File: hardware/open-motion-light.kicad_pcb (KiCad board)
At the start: 2 copper layers, 77 x 73 mm, 89 parts, among them J1 TYPE-C-31-M-12, J2 Conn_01x04, Q1 2N7002, SW1 SW_Push, SW2 SW_Push, SW3 SSSS213800, U1 CN3058E, U2 STM32L031G6U6, U3 MT9284BS6, U4 PIR223D-S0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

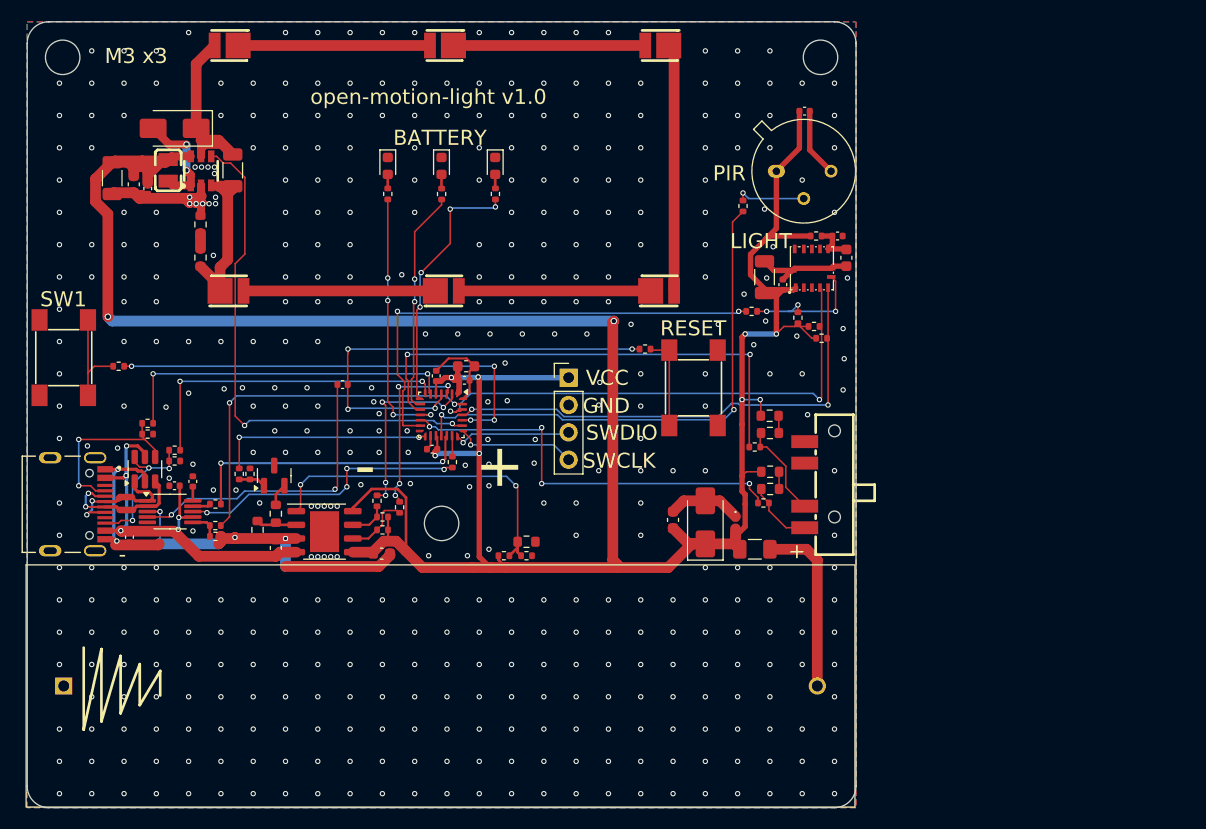
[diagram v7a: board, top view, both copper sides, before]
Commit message: Start updating placement and routing for v1.1
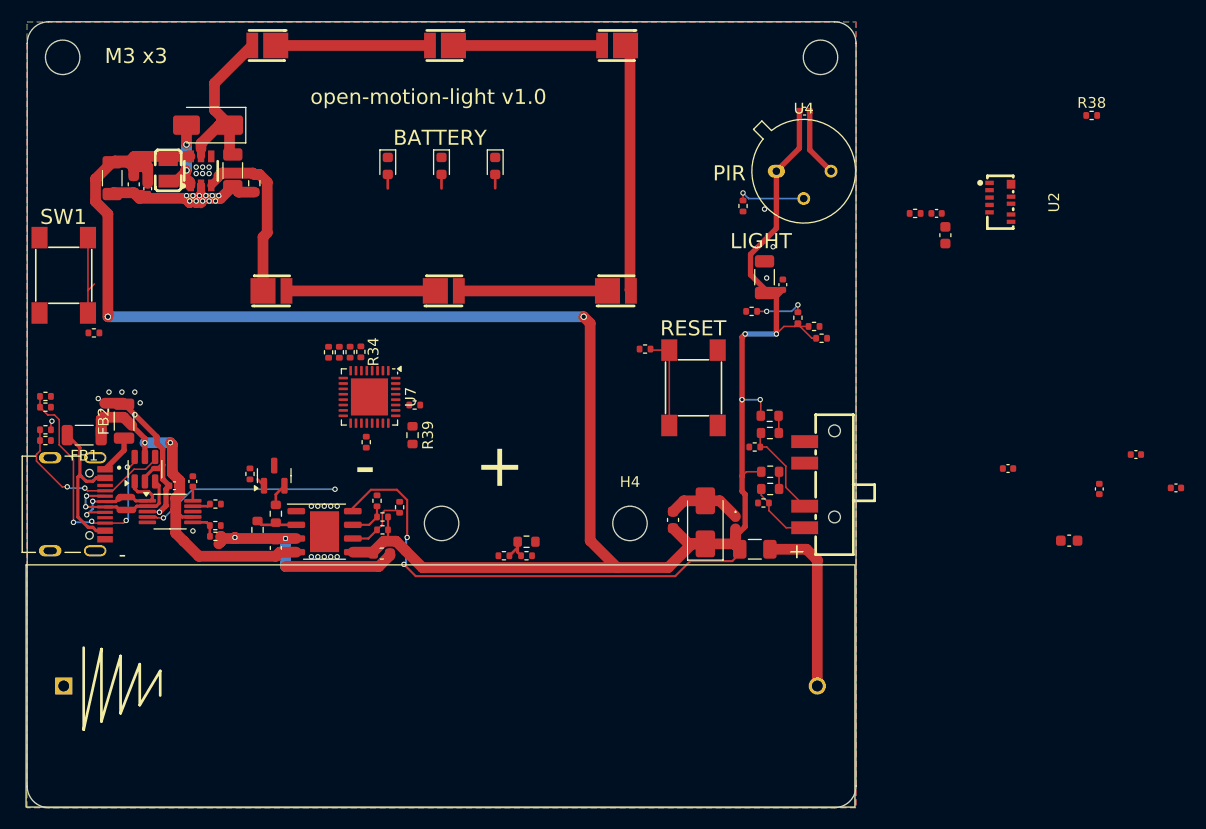
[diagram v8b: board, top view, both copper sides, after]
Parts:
- removed J2: Conn_01x04, Connector_PinHeader_2.54mm:PinHeader_1x04_P2.54mm_Vertical
- removed U5: VCNL4010-GS08, Homebrew:SENSORS-SMD_VCNL4010-GS08
- added FB1: 0R, Inductor_SMD:L_1206_3216Metric, F.Cu at (56.3, 101.4)
- added FB2: 0R, Inductor_SMD:L_1206_3216Metric, F.Cu at (60.0, 100.1)
- added H4: MountingHole, MountingHole:MountingHole_3.2mm_M3_ISO7380, F.Cu at (107.0, 109.6)
- added R38: 100k, Resistor_SMD:R_0402_1005Metric, F.Cu at (149.9, 71.7)
- added R39: 2M, Resistor_SMD:R_0603_1608Metric, F.Cu at (86.8, 101.4)
- added U7: STM32L051K8Ux, Package_DFN_QFN:QFN-32-1EP_5x5mm_P0.5mm_EP3.45x3.45mm, F.Cu at (82.8, 97.8)
- C1: value 10uF -> 4.7uF
- R1: value 2k7 -> 24k
- R2: value 2k7 -> 1k2
- R25: value 2Ω -> 5Ω1
- R34: value 2Ω -> 1k; footprint Resistor_SMD:R_0603_1608Metric -> Resistor_SMD:R_0402_1005Metric
- U2: value STM32L031G6U6 -> VCNL4020-GS08; footprint Package_DFN_QFN:QFN-28_4x4mm_P0.5mm -> Homebrew:SENSOR-SMD_VCNL4020-GS08
- U4: footprint Package_TO_SOT_THT:TO-5-3_Window -> Homebrew:PIR223D-S0
- moved C6 69.2 mm to (157.7, 106.3)
- moved C5 62.8 mm to (154.0, 103.2)
- moved C7 62.5 mm to (150.6, 106.4)
- moved C17 62.3 mm to (142.1, 104.5)
- moved C4 58.3 mm to (147.8, 111.2)
- moved U2 55.6 mm to (141.4, 79.8)
- moved R14 20.0 mm to (81.0, 93.7)
- moved R34 19.0 mm to (82.0, 93.7), turned to -90 degrees
- moved R10 17.5 mm to (87.0, 98.6), turned to 180 degrees
- moved R15 17.5 mm to (80.0, 93.7)
- moved R16 15.7 mm to (79.0, 93.7)
- moved R12 13.0 mm to (52.7, 97.8)
- moved R4 13.0 mm to (52.7, 98.8)
- moved C2 12.0 mm to (58.2, 99.1), turned to 90 degrees
- moved R11 9.51 mm to (52.7, 100.9)
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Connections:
- C11 pad 2: Net-(U3-FB) -> GND
- C12 pad 2: Net-(U5-VDD) -> Net-(U2-VDD)
- C17 pad 2: Net-(U2-NRST) -> Net-(U7-NRST)
- C20 pad 1: Net-(U5-VDD) -> Net-(U2-VDD)
- J1 pad A1B12: GND -> Net-(FB2-Pad1)
- J1 pad A4B9: +5V -> Net-(FB1-Pad2)
- J1 pad B1A12: GND -> Net-(FB2-Pad1)
- J1 pad B4A9: +5V -> Net-(FB1-Pad2)
- L2 pad 1: VCC -> Net-(D8-A)
- L2 pad 2: Net-(D8-A) -> VCC
- R13 pad 2: Net-(U2-NRST) -> Net-(U7-NRST)
- R18 pad 2: Net-(U5-INT) -> Net-(U2-INT)
- R25 pad 2: Net-(R25-Pad2) -> GND
- R27 pad 1: Net-(U5-INT) -> Net-(U2-INT)
- R32 pad 1: VCC -> +5V
- R34 pad 1: Net-(R25-Pad2) -> Net-(U3-EN)
- R34 pad 2: GND -> /WHITE_LED
- R37 pad 2: Net-(U5-VDD) -> Net-(U2-VDD)
- U2 pad 10: /POWER_AUTO -> unconnected-(U2-IRcathode-Pad10)
- U2 pad 2: /~{CHRG} -> /SDA
- U2 pad 3: /~{DONE} -> Net-(U2-INT)
- U2 pad 4: Net-(U2-NRST) -> /SCL
- U2 pad 5: VCC -> Net-(U2-VDD)
- U2 pad 6: /CC1 -> unconnected-(U2-NC-Pad6)
- U2 pad 7: /CC2 -> unconnected-(U2-NC-Pad7)
- U2 pad 8: /LED1 -> GND
- U2 pad 9: /LED2 -> GND
- U3 pad 4: /WHITE_LED -> Net-(U3-EN)
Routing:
- net /PIR: track 48.8 -> 0.00 mm, vias 2 -> 0
- net /WHITE_LED: track 48.3 -> 0.00 mm, vias 2 -> 0
- net /SDA: track 47.3 -> 0.00 mm, vias 2 -> 0
- net /POWER_AUTO: track 46.4 -> 0.00 mm, vias 2 -> 0
- net /SCL: track 45.9 -> 0.00 mm, vias 2 -> 0
- net /LIGHT_INT: track 45.1 -> 0.00 mm, vias 2 -> 0
- net Net-(U2-NRST): track 42.4 -> 0.00 mm, vias 4 -> 0
- net /BUTTON: track 42.4 -> 0.00 mm, vias 4 -> 0
- net /POWER_ON: track 38.5 -> 0.00 mm, vias 4 -> 0
- net /BOOT0: track 33.9 -> 0.00 mm, vias 2 -> 0
- net /CC1: track 32.1 -> 0.84 mm, vias 2 -> 1
- net GND: track 104.5 -> 73.9 mm, vias 453 -> 40
- net /CC2: track 30.1 -> 0.00 mm, vias 2 -> 0
- net /TEMP: track 31.7 -> 3.05 mm, vias 2 -> 0
- net /USART_TX: track 27.0 -> 0.00 mm, vias 2 -> 0
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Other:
- board text removed: "GND"
- board text removed: "SWCLK"
- board text removed: "SWDIO"
- board text removed: "VCC"
